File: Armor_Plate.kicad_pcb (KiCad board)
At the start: 2 copper layers, 135 x 125.1 mm, 46 parts, among them SW3 SW_SP3T

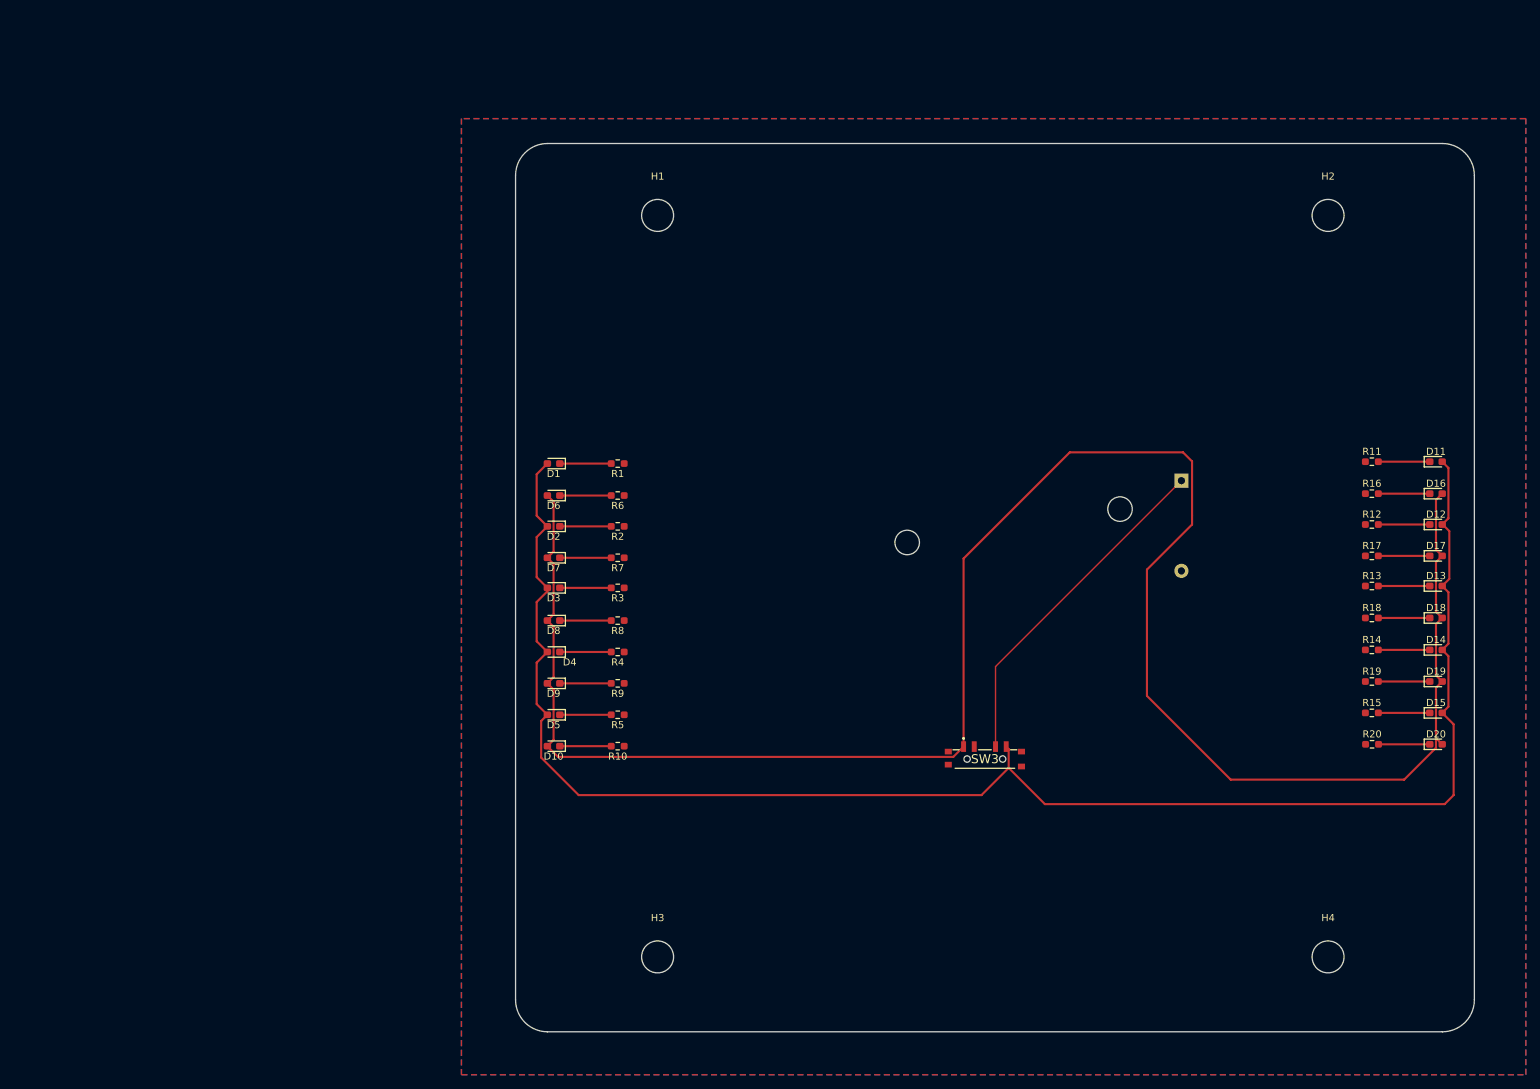
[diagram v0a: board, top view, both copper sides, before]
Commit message: Staged work for Armor Plate team
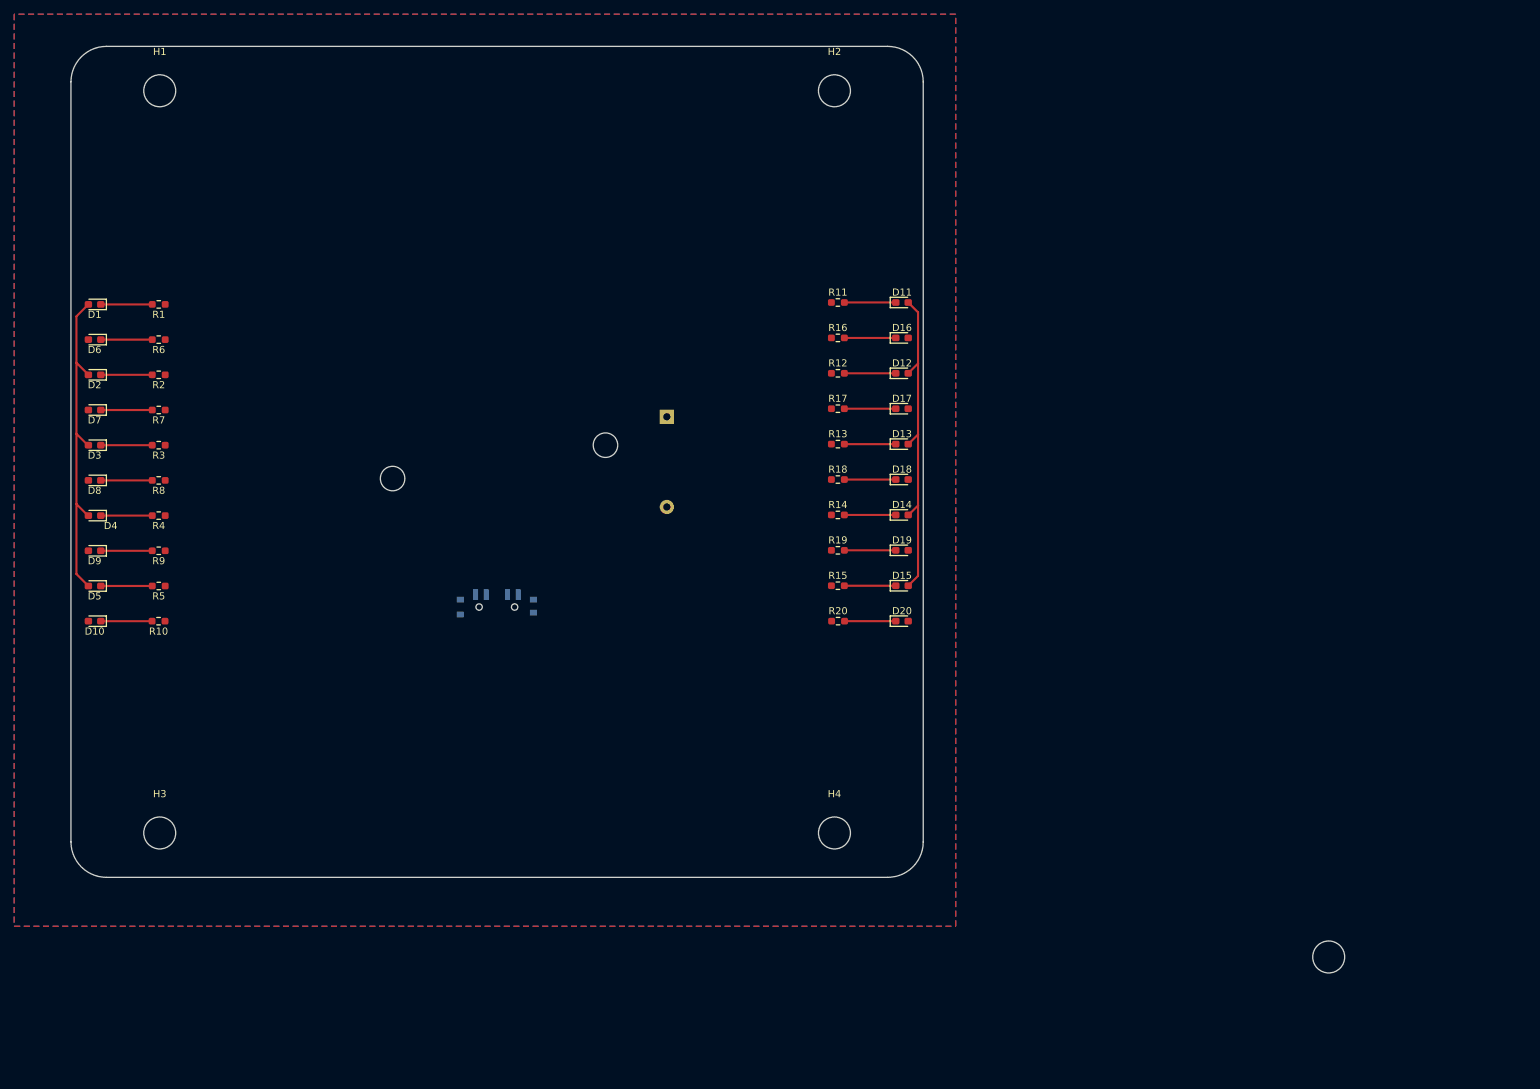
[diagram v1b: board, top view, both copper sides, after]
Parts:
- added ?: , , F.Cu at (197.0, 144.7)
- SW3: moved to B.Cu
- moved D11 78.5 mm to (137.0, 52.6)
- moved R11 78.5 mm to (127.9, 52.6)
- moved D16 78.3 mm to (137.0, 57.5)
- moved R16 78.3 mm to (127.9, 57.5)
- moved D12 78.1 mm to (137.0, 62.5)
- moved R12 78.1 mm to (127.9, 62.5)
- moved D17 78.0 mm to (137.0, 67.5)
- moved R17 78.0 mm to (127.9, 67.5)
- moved D13 77.8 mm to (137.0, 72.5)
- moved R13 77.8 mm to (127.9, 72.5)
- moved D18 77.7 mm to (137.0, 77.5)
- moved R18 77.7 mm to (127.9, 77.5)
- moved D14 77.6 mm to (137.0, 82.5)
- moved R14 77.6 mm to (127.9, 82.5)
- moved D19 77.4 mm to (137.0, 87.5)
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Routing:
- net /3V blue: track 286.0 -> 0.00 mm
- net /3V Red: track 235.5 -> 95.0 mm
- net Net-(BT1-+): track 48.3 -> 0.00 mm
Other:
- board size 135 x 125.1 mm -> 120 x 117 mm
